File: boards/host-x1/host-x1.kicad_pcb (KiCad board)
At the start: 4 copper layers, 91 x 83 mm, 231 parts, among them J1 CONN_3_PWROUT, J2 XILINX_JTAG, J3 STARSHIPRAIDER_IOBOARD_HOST, J4 BEL_FUSE_0826-1G1T-23-F, J5 PMOD_HEADER, M1 LOGO_LONGTHING, M2 LOGO_ROHS, M3 LOGO_WEEE, M4 HOLE, M5 HOLE, M6 HOLE, M7 HOLE, Q1 SSM6N58NU, Q2 SSM6N58NU, Q3 SSM6N58NU, Q4 SSM6N58NU, SW1 SW_Push, U1 OLK-T_3-W12P-C, U10 DSC6102CI2A-100.0000, U11 S25FS064S_BGA, U2 XC7A100T-1FTG256C, U3 LTC3374-QFN, U4 S27KS0641DPBHI02, U5 S27KS0641DPBHI02, U6 S27KS0641DPBHI02, U7 S27KS0641DPBHI02, U8 KSZ9031RN, U9 DSC6101CI2A-025.0000

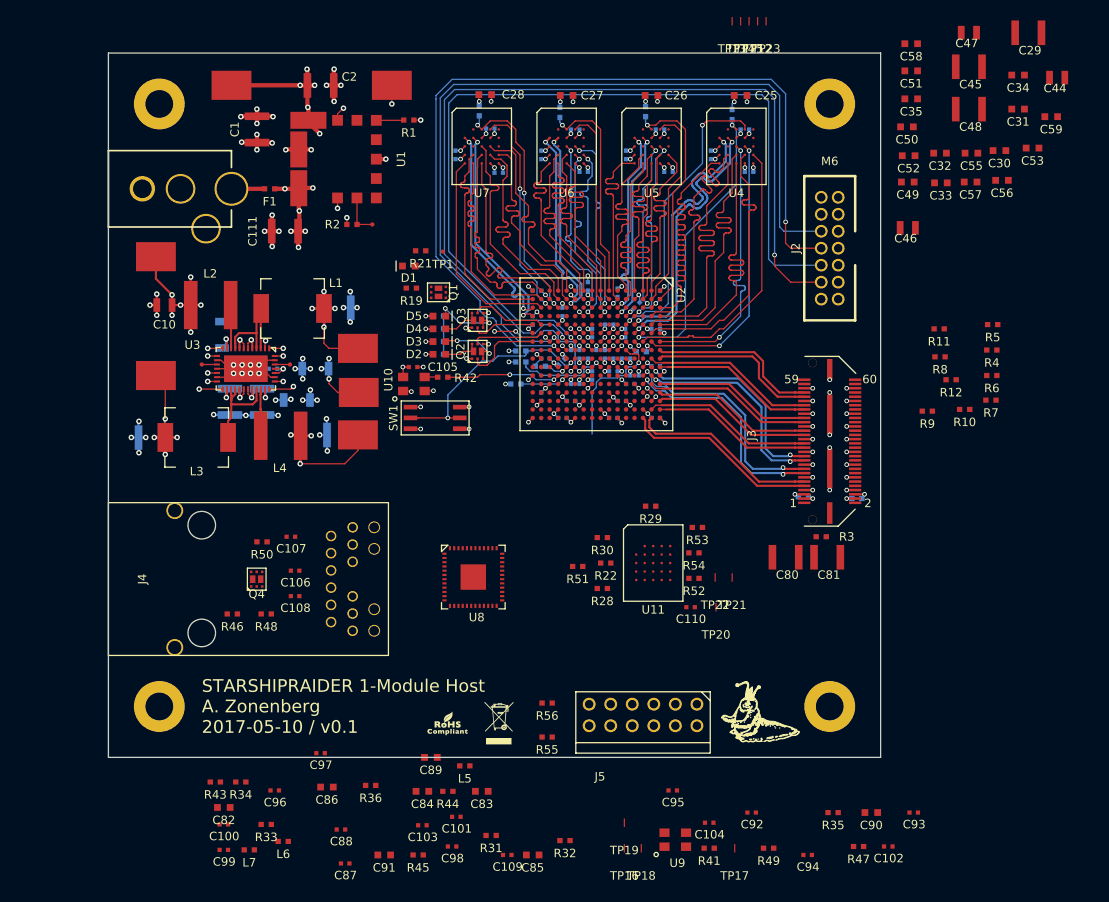
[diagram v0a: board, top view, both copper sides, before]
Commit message: Began routing Ethernet. Lots of tweaks to power plane layout.
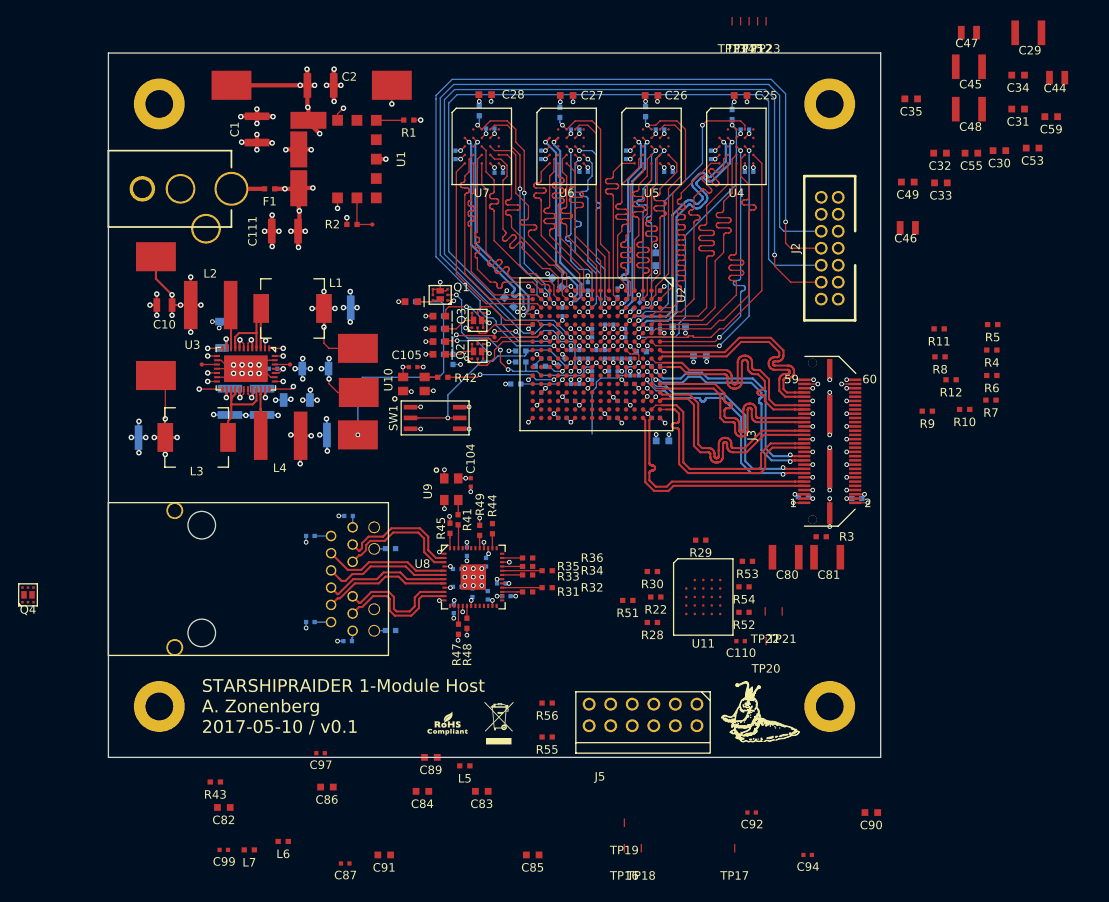
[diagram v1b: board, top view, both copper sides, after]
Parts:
- C100, C101, C102, C103, C106, C107, C108, C109, C50, C51, C52, C56, C57, C58, C88, C93, C95, C96, C98, R19, R21, R46, R50: moved to B.Cu
- moved C57 56.2 mm to (76.2, 47.4), turned to 135 degrees
- moved C102 55.7 mm to (73.7, 81.9), turned to 90 degrees
- moved C93 54.4 mm to (75.9, 82.0)
- moved R47 53.7 mm to (70.2, 85.9), turned to 90 degrees
- moved R49 50.6 mm to (72.8, 74.2), turned to 270 degrees
- moved C56 50.4 mm to (94.3, 63.7)
- moved U9 49.0 mm to (69.4, 69.4), turned to 270 degrees
- moved C104 49.0 mm to (71.7, 68.6), turned to 270 degrees
- moved R41 48.7 mm to (70.2, 73.0), turned to 90 degrees
- moved C51 48.6 mm to (81.8, 45.0), turned to 315 degrees
- moved R35 46.2 mm to (78.4, 78.5), turned to 180 degrees
- moved R34 43.9 mm to (80.7, 79.0), turned to 180 degrees
- moved C58 43.1 mm to (96.2, 50.2), turned to 180 degrees
- moved R33 42.6 mm to (78.4, 79.5), turned to 180 degrees
- moved C100 39.2 mm to (70.1, 80.9)
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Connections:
- U8 pad 10: /Flash / Ethernet/ETH_D_P -> /Flash / Ethernet/ETH_D_N
- U8 pad 11: /Flash / Ethernet/ETH_D_N -> /Flash / Ethernet/ETH_D_P
- U8 pad 5: /Flash / Ethernet/ETH_B_P -> /Flash / Ethernet/ETH_B_N
- U8 pad 6: /Flash / Ethernet/ETH_B_N -> /Flash / Ethernet/ETH_B_P
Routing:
- net /3V3: track 65.3 -> 241.9 mm, vias 11 -> 16
- net /GND: track 764.2 -> 934.9 mm, vias 137 -> 169
- net /5V0: track 110.9 -> 235.9 mm, vias 26 -> 28
- net /12V0_FUSED: track 47.7 -> 168.9 mm, vias 11 -> 13
- net /1V2: track 30.9 -> 133.4 mm, vias 6 -> 12
- net /1V8: track 337.6 -> 404.8 mm, vias 46 -> 58
- net /FPGA support/FPGA_DONE: track 10.9 -> 27.2 mm, vias 1 -> 4
- net /Flash / Ethernet/ETH_C_N: track 0.00 -> 15.1 mm
- net /Flash / Ethernet/ETH_C_P: track 0.00 -> 15.1 mm
- net /Flash / Ethernet/ETH_D_N: track 0.00 -> 15.0 mm
- net /Flash / Ethernet/ETH_D_P: track 0.00 -> 15.0 mm
- net /Flash / Ethernet/ETH_A_N: track 0.00 -> 15.0 mm
- net /Flash / Ethernet/ETH_A_P: track 0.00 -> 15.0 mm
- net /Flash / Ethernet/ETH_B_P: track 0.00 -> 15.0 mm
- net /Flash / Ethernet/ETH_B_N: track 0.00 -> 15.0 mm
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
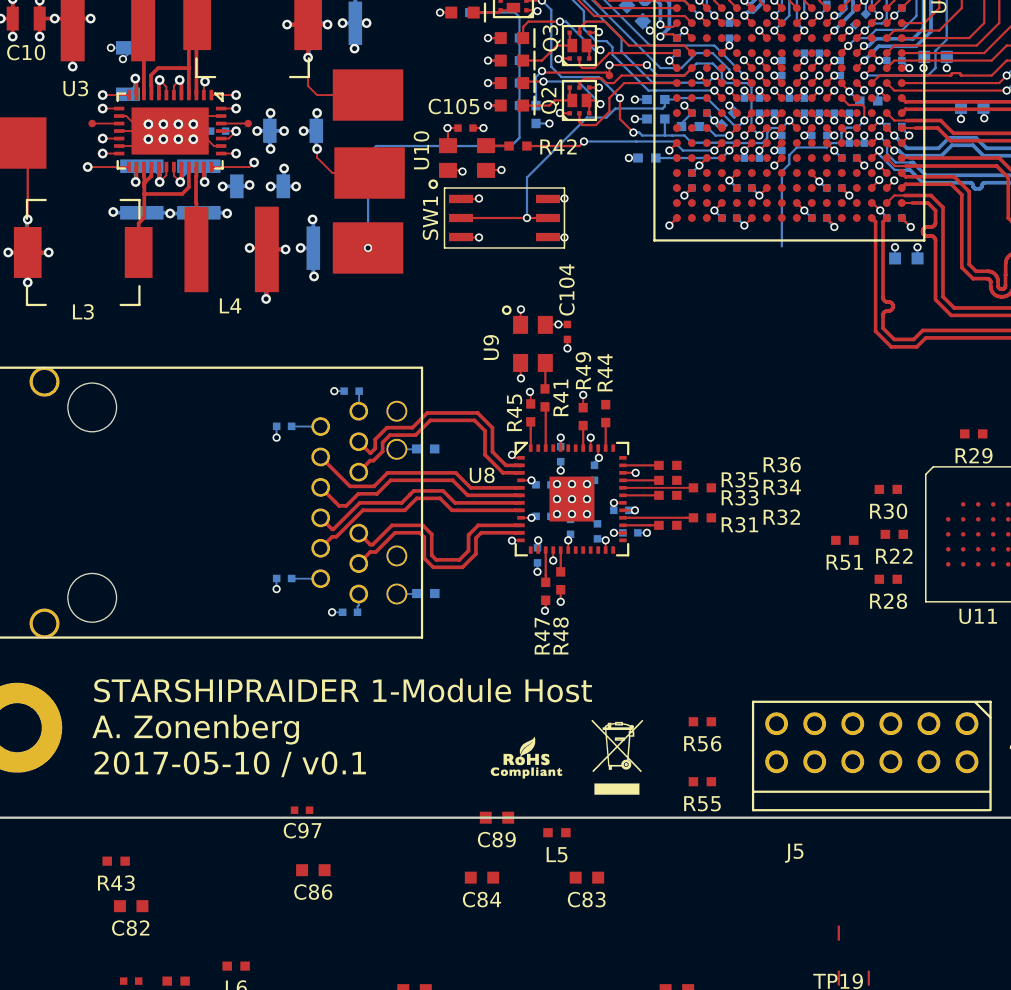
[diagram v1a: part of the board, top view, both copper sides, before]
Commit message: Finished initial RGMII routing
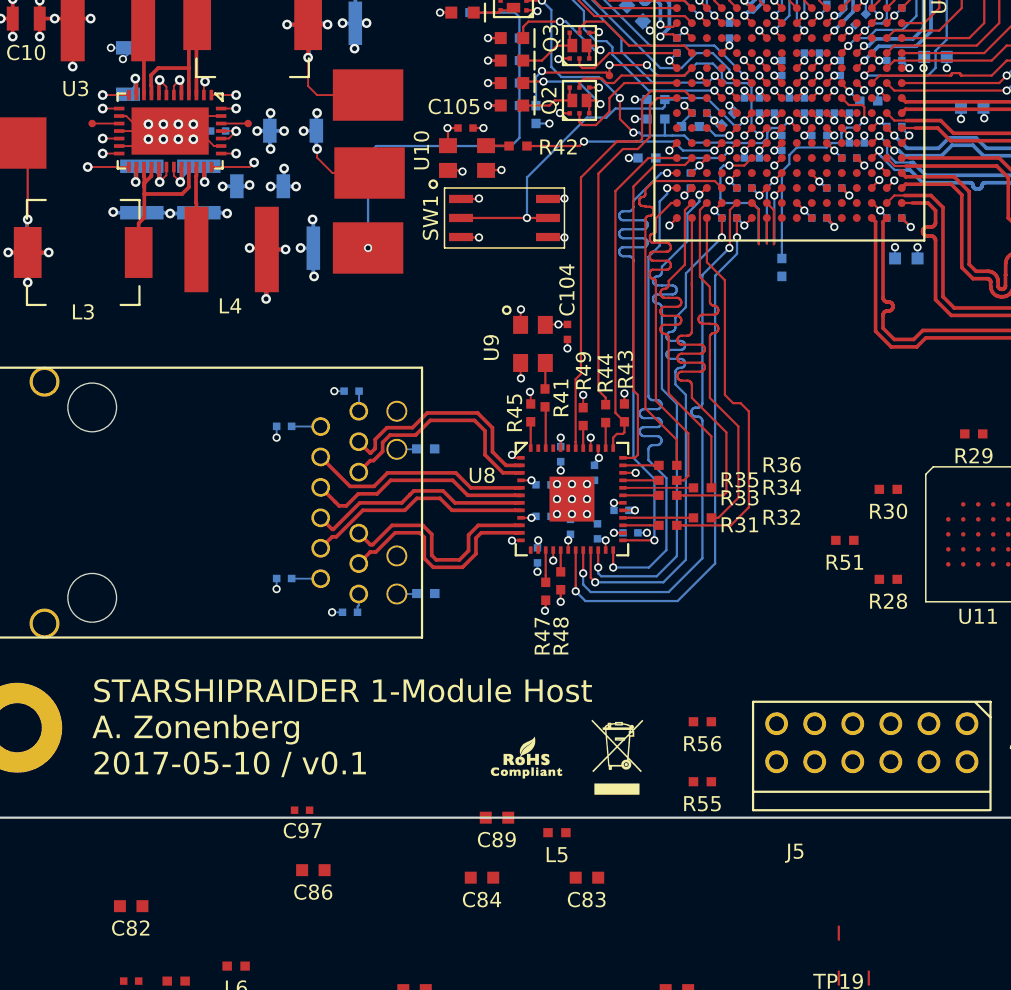
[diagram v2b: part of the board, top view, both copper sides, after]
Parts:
- R22: moved to B.Cu
- moved R43 45.2 mm to (75.5, 74.0), turned to 90 degrees
- moved R22 19.3 mm to (86.0, 64.3), turned to 270 degrees
- moved C71 0.10 mm to (79.9, 58.5)
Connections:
- U2 pad M15: Net-(U2-PadM15) -> /Flash / Ethernet/RGMII_TXD1
- U2 pad M16: Net-(U2-PadM16) -> /Flash / Ethernet/RGMII_TXD0
- U2 pad N13: /Flash / Ethernet/RGMII_RXD0 -> /Flash / Ethernet/ETH_LINK_LED
- U2 pad N16: /Flash / Ethernet/ETH_INT_N -> /Flash / Ethernet/RGMII_TXD2
- U2 pad P10: /Flash / Ethernet/RGMII_TXD3 -> Net-(U2-PadP10)
- U2 pad P11: /Flash / Ethernet/RGMII_TXD2 -> Net-(U2-PadP11)
- U2 pad P13: /Flash / Ethernet/RGMII_RX_DV -> /Flash / Ethernet/ETH_ACTIVITY_LED
- U2 pad P14: Net-(U2-PadP14) -> /Flash / Ethernet/RGMII_TXD3
- U2 pad P15: /Flash / Ethernet/ETH_RST_N -> /Flash / Ethernet/RGMII_RXD2
- U2 pad P16: /Flash / Ethernet/ETH_ACTIVITY_LED -> /Flash / Ethernet/RGMII_RXD3
- U2 pad R10: /Flash / Ethernet/ETH_MDIO -> Net-(U2-PadR10)
- U2 pad R11: /Flash / Ethernet/ETH_MDC -> Net-(U2-PadR11)
- U2 pad R12: /Flash / Ethernet/RGMII_TXD1 -> /Flash / Ethernet/ETH_MDC
- U2 pad R13: /Flash / Ethernet/RGMII_TX_EN -> Net-(U2-PadR13)
- U2 pad R15: /Flash / Ethernet/ETH_LINK_LED -> /Flash / Ethernet/RGMII_RXD0
- U2 pad R16: /Flash / Ethernet/RGMII_RXD3 -> /Flash / Ethernet/RGMII_RXD1
- U2 pad R8: Net-(U2-PadR8) -> /Flash / Ethernet/ETH_RST_N
- U2 pad T12: /Flash / Ethernet/RGMII_TXD0 -> /Flash / Ethernet/ETH_MDIO
- U2 pad T13: /Flash / Ethernet/RGMII_TX_CLK -> /Flash / Ethernet/RGMII_TX_EN
- U2 pad T14: /Flash / Ethernet/RGMII_RXD2 -> /Flash / Ethernet/RGMII_TX_CLK
- U2 pad T15: /Flash / Ethernet/RGMII_RXD1 -> /Flash / Ethernet/RGMII_RX_DV
- U2 pad T8: Net-(U2-PadT8) -> /Flash / Ethernet/ETH_INT_N
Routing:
- net /Flash / Ethernet/RGMII_TX_CLK: track 0.00 -> 37.0 mm, vias 0 -> 2
- net /Flash / Ethernet/RGMII_TXD0: track 0.00 -> 37.0 mm, vias 0 -> 2
- net /Flash / Ethernet/RGMII_TXD3: track 0.00 -> 37.0 mm, vias 0 -> 2
- net /Flash / Ethernet/RGMII_TXD2: track 0.00 -> 37.0 mm, vias 0 -> 2
- net /Flash / Ethernet/RGMII_TX_EN: track 0.00 -> 37.0 mm, vias 0 -> 2
- net /Flash / Ethernet/RGMII_TXD1: track 0.00 -> 37.0 mm, vias 0 -> 2
- net /Flash / Ethernet/RGMII_RXD1: track 0.00 -> 30.6 mm
- net /Flash / Ethernet/ETH_RST_N: track 0.00 -> 29.7 mm
- net /Flash / Ethernet/RGMII_RX_CLK: track 0.00 -> 26.1 mm
- net /Flash / Ethernet/RGMII_RXD3: track 0.00 -> 26.1 mm
- net /Flash / Ethernet/RGMII_RXD2: track 0.00 -> 26.1 mm
- net /Flash / Ethernet/RGMII_RXD0: track 0.00 -> 26.0 mm
- net /Flash / Ethernet/RGMII_RX_DV: track 0.00 -> 26.0 mm
- net /Flash / Ethernet/ETH_INT_N: track 0.00 -> 24.2 mm
- net /Flash / Ethernet/ETH_MDC: track 0.00 -> 23.8 mm
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
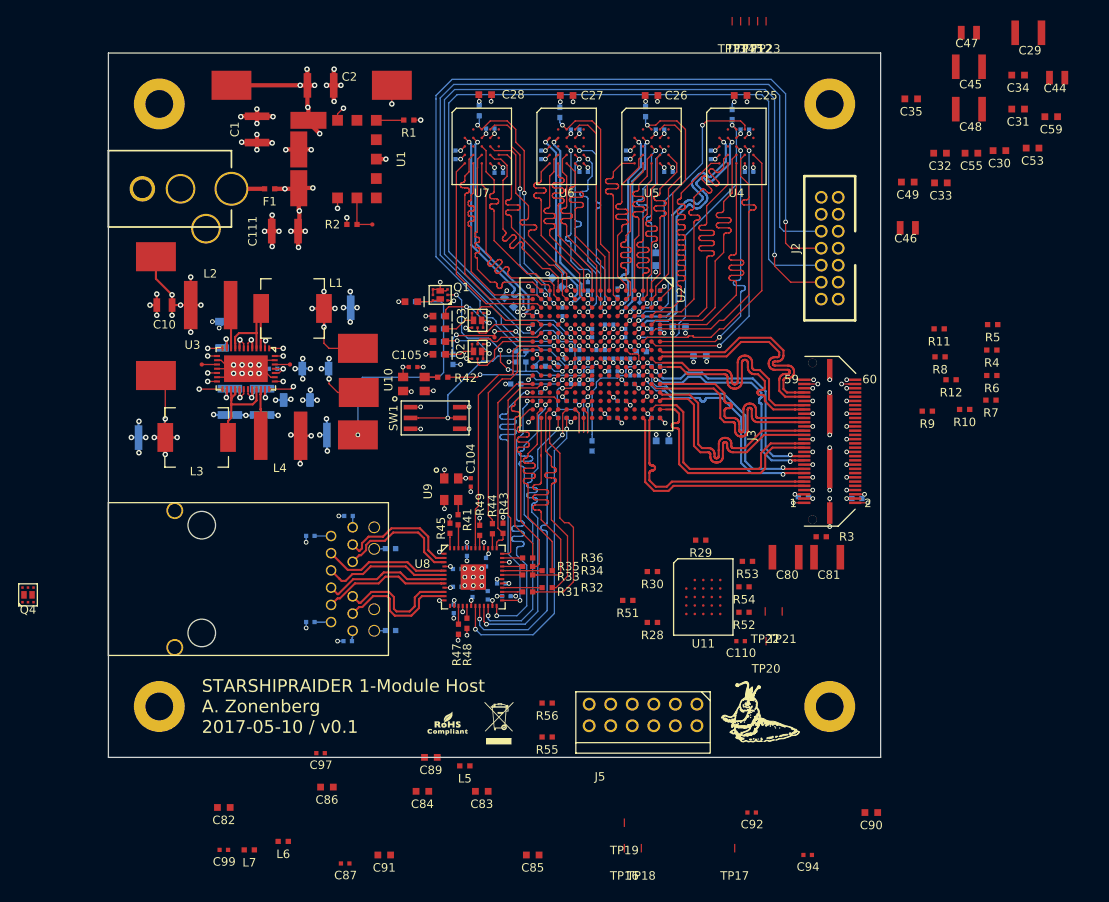
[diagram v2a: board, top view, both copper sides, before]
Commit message: Continued work on Ethernet power stuff. Now down to 100 unrouted nets
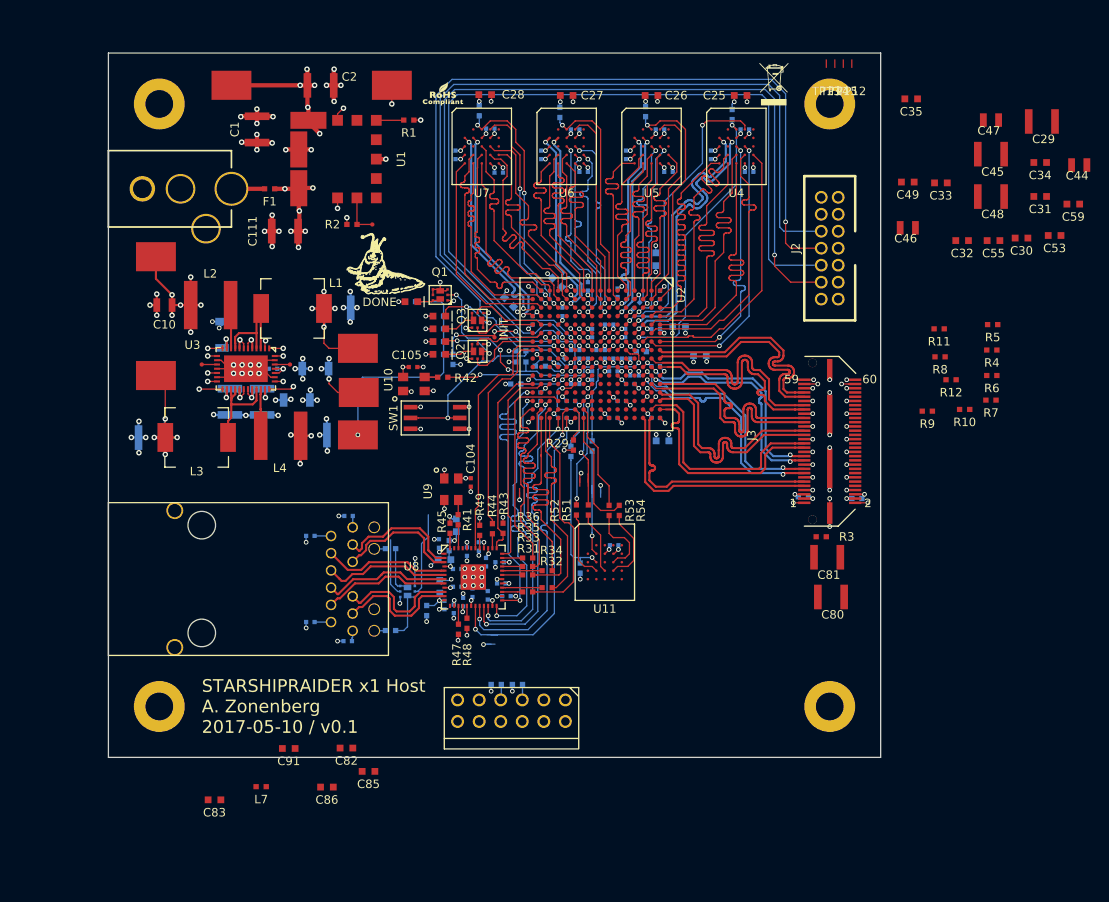
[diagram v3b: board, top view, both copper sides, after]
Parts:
- C110, C84, C87, C89, C90, C92, C94, C97, C99, L5, L6, Q4, R28, R30, R55, R56, TP16, TP17, TP20, TP21: moved to B.Cu
- moved M3 82.0 mm to (107.4, 21.7)
- moved M2 74.2 mm to (68.5, 22.8)
- moved M1 68.8 mm to (62.2, 43.2)
- moved TP23 58.7 mm to (84.3, 68.6)
- moved C90 58.5 mm to (68.6, 77.7), turned to 180 degrees
- moved C94 52.0 mm to (68.6, 83.0), turned to 270 degrees
- moved C92 44.9 mm to (72.7, 76.2), turned to 270 degrees
- moved Q4 44.7 mm to (64.2, 81.5), turned to 270 degrees
- moved C99 44.1 mm to (68.0, 75.8), turned to 90 degrees
- moved TP18 44.0 mm to (78.5, 69.8)
- moved TP19 40.9 mm to (77.5, 69.8)
- moved L6 40.0 mm to (69.2, 76.0), turned to 90 degrees
- moved C87 39.9 mm to (75.1, 78.0), turned to 180 degrees
- moved TP17 37.4 mm to (74.1, 87.7), turned to 90 degrees
- moved C84 31.6 mm to (70.0, 73.7), turned to 90 degrees
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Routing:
- net /GND: track 934.9 -> 1017.6 mm, vias 169 -> 184
- net /1V8: track 408.6 -> 430.4 mm, vias 59 -> 61
- net /3V3: track 241.9 -> 261.1 mm, vias 16 -> 19
- net /Flash / Ethernet/FLASH_CS_N: track 0.00 -> 15.6 mm, vias 0 -> 1
- net /FLASH_SCK: track 0.00 -> 13.2 mm, vias 0 -> 1
- net /Flash / Ethernet/FLASH_DQ3: track 1.70 -> 14.2 mm
- net /Flash / Ethernet/FLASH_DQ0: track 5.11 -> 15.2 mm, vias 1 -> 2
- net /Flash / Ethernet/ETH_LINK_LED: track 0.00 -> 9.94 mm
- net /Flash / Ethernet/FLASH_DQ2: track 2.96 -> 12.5 mm
- net /Flash / Ethernet/FLASH_DQ1: track 3.91 -> 13.0 mm, vias 1 -> 2
- net Net-(R54-Pad2): track 0.00 -> 8.90 mm
- net Net-(R53-Pad2): track 0.00 -> 8.57 mm
- net Net-(R52-Pad2): track 0.00 -> 8.05 mm
- net Net-(R51-Pad2): track 0.00 -> 7.36 mm
- net /Flash / Ethernet/ETH_ACTIVITY_LED: track 0.00 -> 6.75 mm
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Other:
- board text added: "DONE"
- board text added: "INIT"
- board text added: "STARSHIPRAIDER x1 Host A. Zonenberg 2017-05-10 / v0.1"
- board text removed: "STARSHIPRAIDER 1-Module Host A. Zonenberg 2017-05-10 / v0.1"
